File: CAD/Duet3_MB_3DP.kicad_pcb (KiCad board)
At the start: 4 copper layers, 101.9 x 125 mm, 261 parts, among them J1 SWD, J16 EXPANSION, J17 ESP_DB, J18 250-502/000-006, J19 A2543WV-5P, J2 A2543WV-2P, J27 uSD_Socket, J30 LASER/VFD, J33 A2543WV-4P, J34 A2543WV-4P, J43 USB, J46 ETHERNET, J48 SBC, J49 A2543WV-2P, J59 A2543WV-2P, J60 A2543WV-2P, M1 FID, M11 MOUNTING, M12 Logo_KICAD, M15 MOUNTING, M2 FID, M3 MOUNTING, M9 MOUNTING, Q1 BC807, Q21 MMBTA06-7-F, Q22 MMBTA06-7-F, U1 SN74F125DR, U11 ATSAME70Q20B-ANT, U13 MCP2542, U16 KSZ8081RNACA, U17 74LVC2G125, U19 74LVC2G34, U2 SN74F125DR, U20 Optoisolator, U21 SN74F125DR, U22 SN74F125DR, U23 Optoisolator, U24 LM70860RRXR, U27 Optoisolator, U28 Optoisolator, U3 EMIF06, U4 AP7361C-33E-13, U5 RClamp0504FB, U6 SN74F125DR, U7 AP22816AKEWT, U9 74HCT365, X1 ECS-120-10-33B-CKM-TR, X2 25Mhz

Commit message: PCB Done
As far as I am aware, everything is done, still needs to be run through JLCDFM.
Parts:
- moved D33 150.9 mm to (100.7, 193.9), turned to 180 degrees
- moved D35 147.7 mm to (96.0, 191.6)
- moved C6 88.4 mm to (111.9, 121.6)
- moved C21 87.2 mm to (109.0, 119.5), turned to -90 degrees
- moved R44 85.9 mm to (106.0, 119.6), turned to 90 degrees
- moved R51 83.0 mm to (107.6, 119.6), turned to 90 degrees
- moved L2 75.5 mm to (95.2, 100.3)
- moved C22 75.2 mm to (100.1, 107.0), turned to 180 degrees
- moved R48 74.2 mm to (110.0, 119.5), turned to 90 degrees
- moved D25 70.0 mm to (132.1, 115.9), turned to 90 degrees
- moved C23 68.2 mm to (100.1, 102.7), turned to 180 degrees
- moved F4 64.3 mm to (131.8, 121.5)
- moved C24 61.8 mm to (105.1, 102.7)
- moved C25 61.8 mm to (105.1, 107.0)
- moved D29 60.5 mm to (135.3, 115.7), turned to 90 degrees
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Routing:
- net 5V_EXT: track 109.8 -> 170.5 mm, vias 1 -> 4
- net V_FUSED_IO: track 13.1 -> 50.7 mm, vias 0 -> 1
- net 5V_INT: track 296.7 -> 326.5 mm
- net (no net): track 14.0 -> 0.00 mm, vias 4 -> 0
- net V_FUSED: track 130.5 -> 140.3 mm, vias 3 -> 2
- net GND: track 380.7 -> 386.9 mm, vias 73 -> 85
- net /Power/CONFIG: track 0.00 -> 5.32 mm
- net UTXD4: track 90.0 -> 94.8 mm
- net /Power/EXTCOMP: track 0.00 -> 4.45 mm
- net /Power/RT: track 0.00 -> 3.96 mm
- net /Power/VIN1: track 3.47 -> 6.83 mm, vias 0 -> 2
- net /Power/C6_1: track 0.00 -> 2.51 mm
- net /Power/5V_Common: track 59.6 -> 62.0 mm
- net VIN_POWER_MON: track 107.3 -> 109.2 mm
- net ESP_DATA_RDY: track 113.1 -> 115.0 mm
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- added copper zone on F.Cu, net /Power/5V_Common
- added copper zone on F.Cu, net /Power/5v_ext_fuse
- added copper zone on F.Cu, net /Power/L2
- added copper zone on F.Cu, net /Power/VIN1
- added copper zone on F.Cu, net 5V_EXT
- added copper zone on B.Cu, net GND
- added copper zone on B.Cu, net V_IN

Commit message: Update Revision
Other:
- board text added: "Duet 3 Mainboard 3DPotter Version Revision v1.50"
- board text removed: "Duet 3 Mainboard 3DPotter Version Revision v1.00"
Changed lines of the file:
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@@
 		(title "Duet 3 MB 6XD")
 		(date "2023-02-22")
-		(rev "1.01")
+		(rev "1.5")
 		(company "Duet3D")
 		(comment 1 "(c) Duet3D")
@@
 		(layer "F.CrtYd")
 	)
-	(gr_text "Duet 3 Mainboard\n3DPotter Version\nRevision v1.00"
+	(gr_text "Duet 3 Mainboard\n3DPotter Version\nRevision v1.50"
 		(at 78.75 188 0)
 		(layer "F.SilkS")

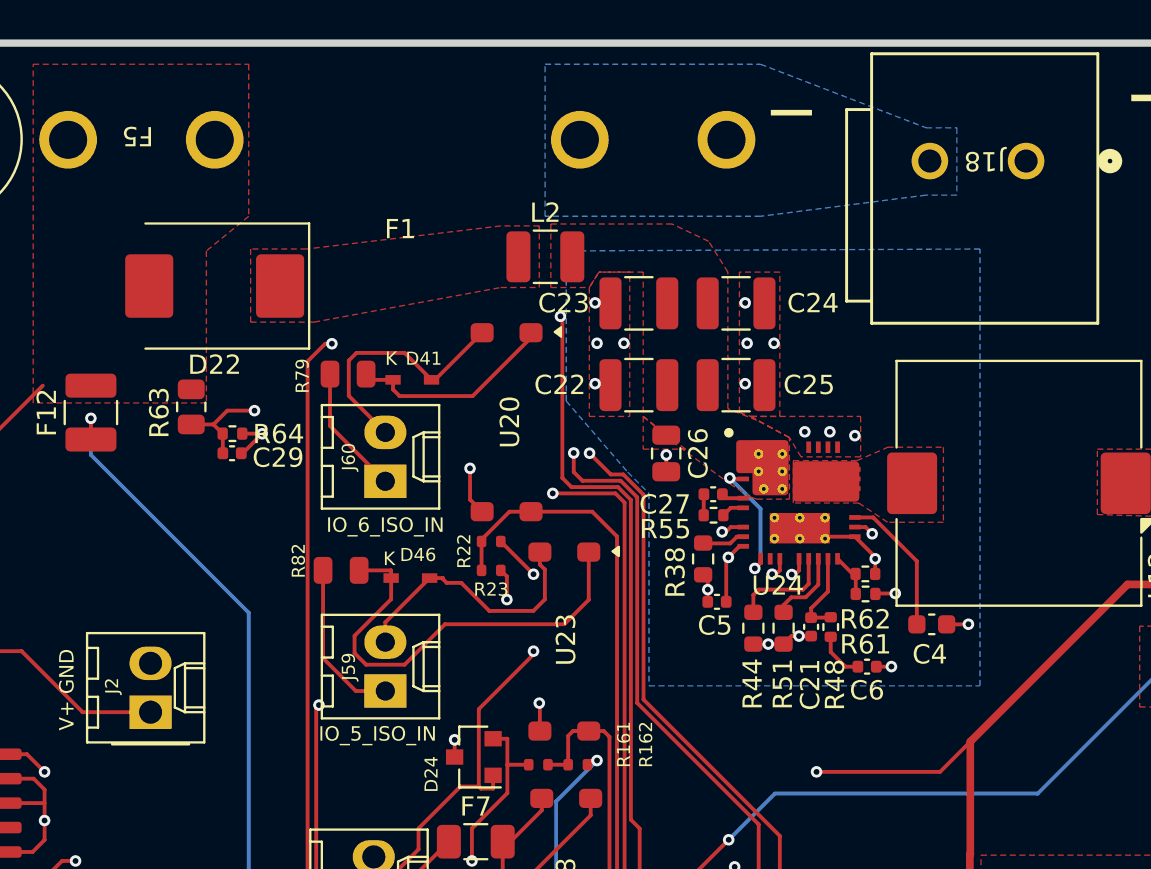
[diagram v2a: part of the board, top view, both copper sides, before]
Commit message: Final Touches?
Top Surface ground plane around LM70860 with star via stitching and some changes for ease of manufacturing.
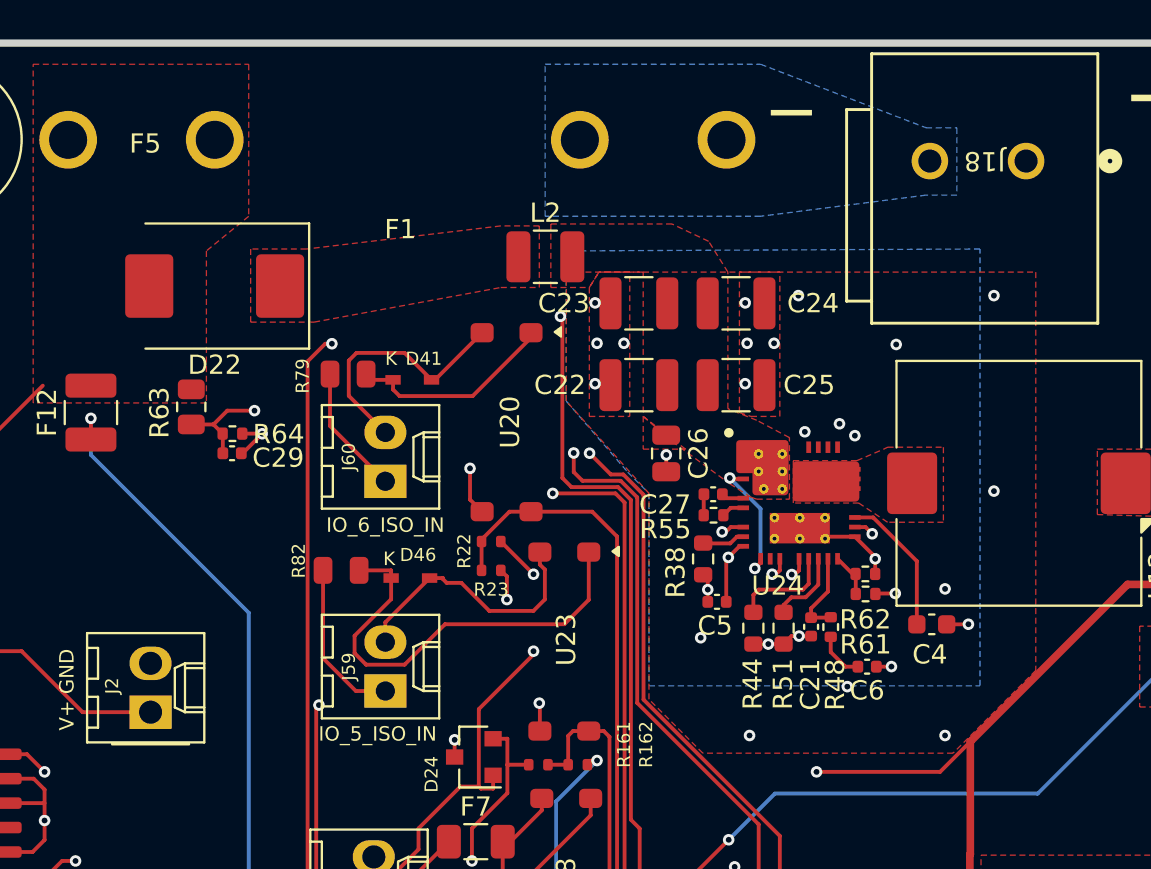
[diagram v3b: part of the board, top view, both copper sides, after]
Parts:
- turned F5 to 0 degrees
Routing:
- net GND: vias 85 -> 94
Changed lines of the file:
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@@
 	(footprint "3DPotter:01220088Z"
 		(layer "F.Cu")
-		(at 74.225 94.225 180)
+		(at 74.225 94.225)
 		(property "Reference" "F5"
-			(at 0.2 0.2 180)
+			(at 0.2 0.2 0)
 			(unlocked yes)
 			(layer "F.SilkS")
@@
 		)
 		(property "Value" "~"
-			(at -0.1 -5.9 180)
+			(at -0.1 -5.9 0)
 			(unlocked yes)
 			(layer "F.Fab")
@@
 		)
 		(property "Datasheet" ""
-			(at 0 0 180)
+			(at 0 0 0)
 			(unlocked yes)
 			(layer "F.Fab")
@@
 		)
 		(property "Description" ""
-			(at 0 0 180)
+			(at 0 0 0)
 			(unlocked yes)
 			(layer "F.Fab")
@@
 		)
 		(property "LCSC" "C206903"
-			(at 0 0 180)
+			(at 0 0 0)
 			(unlocked yes)
 			(layer "F.Fab")
@@
 		)
 		(property "Part Number" "01220088Z"
-			(at 0 0 180)
+			(at 0 0 0)
 			(unlocked yes)
 			(layer "F.Fab")
@@
 		)
 		(fp_text user "${REFERENCE}"
-			(at 0 -4.8 180)
+			(at 0 -4.8 0)
 			(unlocked yes)
 			(layer "F.Fab")
@@
 		)
 		(pad "1" thru_hole circle
-			(at -3.81 0 180)
+			(at -3.81 0)
 			(size 3 3)
 			(drill 1.98)
@@
 		)
 		(pad "1" thru_hole circle
-			(at 3.81 0 180)
+			(at 3.81 0)
 			(size 3 3)
 			(drill 1.98)
@@
 	)
 	(via
+		(at 118.526904 102.32175)
+		(size 0.6)
+		(drill 0.3)
+		(layers "F.Cu" "B.Cu")
+		(free yes)
+		(net 1)
+	)
+	(via
 		(at 123.5 174.4)
 		(size 0.6)
@@
 	)
 	(via
+		(at 103.286904 120.10175)
+		(size 0.6)
+		(drill 0.3)
+		(layers "F.Cu" "B.Cu")
+		(free yes)
+		(net 1)
+	)
+	(via
 		(at 94 201.5)
 		(size 0.6)
@@
 	)
 	(via
+		(at 118.526904 112.48175)
+		(size 0.6)
+		(drill 0.3)
+		(layers "F.Cu" "B.Cu")
+		(free yes)
+		(net 1)
+	)
+	(via
 		(at 139.1 136.2)
 		(size 0.6)
@@
 	)
 	(via
+		(at 115.986904 117.56175)
+		(size 0.6)
+		(drill 0.3)
+		(layers "F.Cu" "B.Cu")
+		(free yes)
+		(net 1)
+	)
+	(via
 		(at 105.952 206.348)
 		(size 0.6)
@@
 	)
 	(via
-		(at 110 109.4)
+		(at 110.5 108.983)
 		(size 0.6)
 		(drill 0.3)
@@
 	)
 	(via
+		(at 113.446904 104.86175)
+		(size 0.6)
+		(drill 0.3)
+		(layers "F.Cu" "B.Cu")
+		(free yes)
+		(net 1)
+	)
+	(via
 		(at 91.3 111.3)
 		(size 0.6)
@@
 	)
 	(via
+		(at 115.986904 125.18175)
+		(size 0.6)
+		(drill 0.3)
+		(layers "F.Cu" "B.Cu")
+		(free yes)
+		(net 1)
+	)
+	(via
 		(at 111.3 109.6)
 		(size 0.6)
@@
 	)
 	(via
+		(at 108.366904 102.32175)
+		(size 0.6)
+		(drill 0.3)
+		(layers "F.Cu" "B.Cu")
+		(free yes)
+		(net 1)
+	)
+	(via
 		(at 103 168.25)
 		(size 0.6)
@@
 	)
 	(via
+		(at 110.906904 122.64175)
+		(size 0.6)
+		(drill 0.3)
+		(layers "F.Cu" "B.Cu")
+		(free yes)
+		(net 1)
+	)
+	(via
 		(at 108.7 109.4)
 		(size 0.6)
@@
 	)
 	(via
+		(at 105.826904 125.18175)
+		(size 0.6)
+		(drill 0.3)
+		(layers "F.Cu" "B.Cu")
+		(free yes)
+		(net 1)
+	)
+	(via
 		(at 69.1917 129.6)
 		(size 0.6)
@@
 	)
 	(zone
-		(net 283)
-		(net_name "/Power/SW")
+		(net 1)
+		(net_name "GND")
 		(layer "F.Cu")
 		(hatch edge 0.5)
-		(priority 3)
 		(connect_pads yes
-			(clearance 0.2)
+			(clearance 0.4)
 		)
-		(min_thickness 0.25)
+		(min_thickness 0.2)
 		(filled_areas_thickness no)
 		(fill yes
@@
 		(polygon
 			(pts
-				(xy 108.1 110.9) (xy 111.4 110.9) (xy 112.8 110.3) (xy 113 110.2) (xy 115.9 110.2) (xy 115.9 114.1)
-				(xy 113 114.1) (xy 111.5 113.1) (xy 108.1 113.100002)
+				(xy 120.7 101.1) (xy 120.7 121.8) (xy 116.4 126.1) (xy 103.4 126.1) (xy 100.6 123.3) (xy 100.6 112.6)
+				(xy 96.3 107.8) (xy 96.3 101.1)
 			)
 		)
 	)
 	(zone
-		(net 100)
-		(net_name "5V_EXT")
+		(net 283)
+		(net_name "/Power/SW")
 		(layer "F.Cu")
 		(hatch edge 0.5)
-		(priority 15)
+		(priority 3)
 		(connect_pads yes
 			(clearance 0.2)
@@
 			(thermal_gap 0.5)
 			(thermal_bridge_width 0.5)
-			(island_removal_mode 1)
-			(island_area_min 10)
 		)
 		(polygon
 			(pts
-				(xy 130.8 123.7) (xy 130.8 119.5) (xy 126.1 119.5) (xy 126.1 123.7)
+				(xy 108.1 110.9) (xy 111.4 110.9) (xy 112.8 110.3) (xy 113 110.2) (xy 115.9 110.2) (xy 115.9 114.1)
+				(xy 113 114.1) (xy 111.5 113.1) (xy 108.1 113.100002)
 			)
 		)
 	)
 	(zone
-		(net 282)
-		(net_name "/Power/ISNS+")
+		(net 100)
+		(net_name "5V_EXT")
 		(layer "F.Cu")
 		(hatch edge 0.5)
-		(priority 5)
+		(priority 15)
 		(connect_pads yes
 			(clearance 0.2)
@@
 			(thermal_gap 0.5)
 			(thermal_bridge_width 0.5)
+			(island_removal_mode 1)
+			(island_area_min 10)
 		)
 		(polygon
 			(pts
-				(xy 123.9 110.3) (xy 127.2 110.3) (xy 129.2 110.1) (xy 129.2 113.9) (xy 127.2 113.8) (xy 123.9 113.7)
+				(xy 130.8 123.7) (xy 130.8 119.5) (xy 126.1 119.5) (xy 126.1 123.7)
 			)
 		)
 	)
 	(zone
-		(net 1)
-		(net_name "GND")
+		(net 282)
+		(net_name "/Power/ISNS+")
 		(layer "F.Cu")
 		(hatch edge 0.5)
-		(priority 11)
+		(priority 5)
 		(connect_pads yes
 			(clearance 0.2)
@@
 			(thermal_gap 0.5)
 			(thermal_bridge_width 0.5)
-			(island_removal_mode 1)
-			(island_area_min 10)
 		)
 		(polygon
 			(pts
-				(xy 105.9 108.6) (xy 111.6 108.6) (xy 111.6 110.7) (xy 108.5 110.7) (xy 107.9 109.7)
+				(xy 123.9 110.3) (xy 127.2 110.3) (xy 129.2 110.1) (xy 129.2 113.9) (xy 127.2 113.8) (xy 123.9 113.7)
 			)
 		)
@@
 		)
 	)
+	(group "ViaStitching GND"
+		(members "08d6cd05-e4b3-4946-b3ed-9f8e8ff4cea7" "32c10978-15b1-4970-a701-e39d6d9bc9b0"
+			"3cdc85de-5f74-4f96-b75c-316ddf120ee5" "44b36923-18e5-494e-9127-6f00e2b2c0ce"
+			"84e47675-af57-447a-8adc-70d630759db9" "b757bc40-2a84-4efe-8398-50961d456169"
+			"cbea062c-2b67-41ce-afe6-898e85d1ec21" "e26bd77d-0175-4a4a-9672-42ba83b905c4"
+			"e770a36b-fd71-47b7-82e2-63066bf0318a"
+		)
+	)

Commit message: Misc. QOL
Moved some vias around, added some vias, etc.
Board passed DFM.
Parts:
- turned J30 to 90 degrees
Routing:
- net /Headers/vfd_conn: track 5.22 -> 8.78 mm
- net GND: track 386.9 -> 387.9 mm
- net 5V_EXT: vias 4 -> 8
- added copper zone on B.Cu, net 5V_EXT
- added copper zone on In2.Cu, net 5V_EXT
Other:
- board text added: "K"
